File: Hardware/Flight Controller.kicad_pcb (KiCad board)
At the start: 6 copper layers, 47.5 x 47.5 mm, 159 parts, among them J1 USB4110GFA, J2 FPV, J3 ST_LINK, J4 GPS, J5 Airspeed sensor, J6 4in1 ESC, J7 RC Receiver, J8 VTX, J9 DJI, Q1 AO3407A, SW1 reset, SW2 MCU_BOOT, U1 TPS54302, U10 BMI270, U12 BMP388, U13 AT7456E, U14 SN65HVD230, U2 USBLC6-2SC6, U3 INA226, U4 AP63205WU, U5 AP2112K-3.3, U6 AP7343-33W5-7, U7 STM32H743VITx, U8 ICM-42688-P, U9 W25Q128JVSIQ, Y1 8MHz 12pF, Y2 27Mhz 20pF

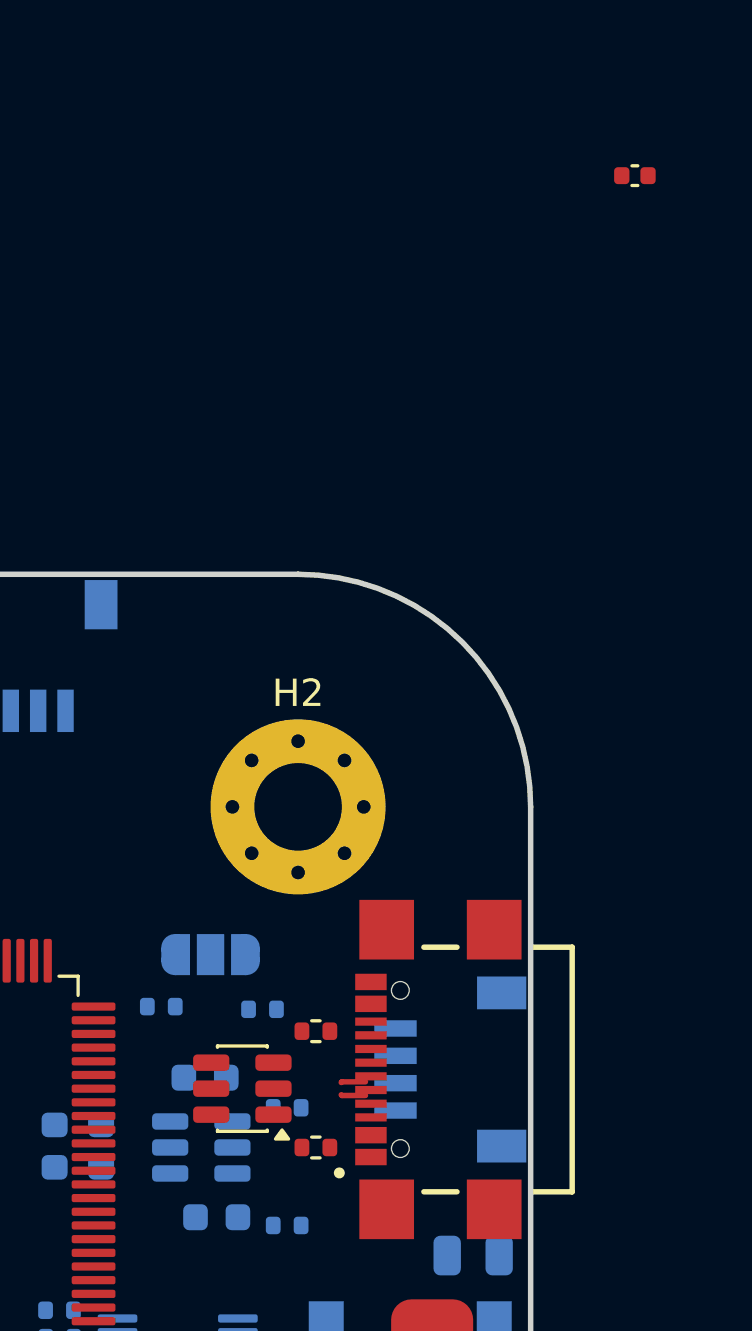
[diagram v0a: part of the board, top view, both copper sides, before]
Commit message: updated wiring of ESD from USB C
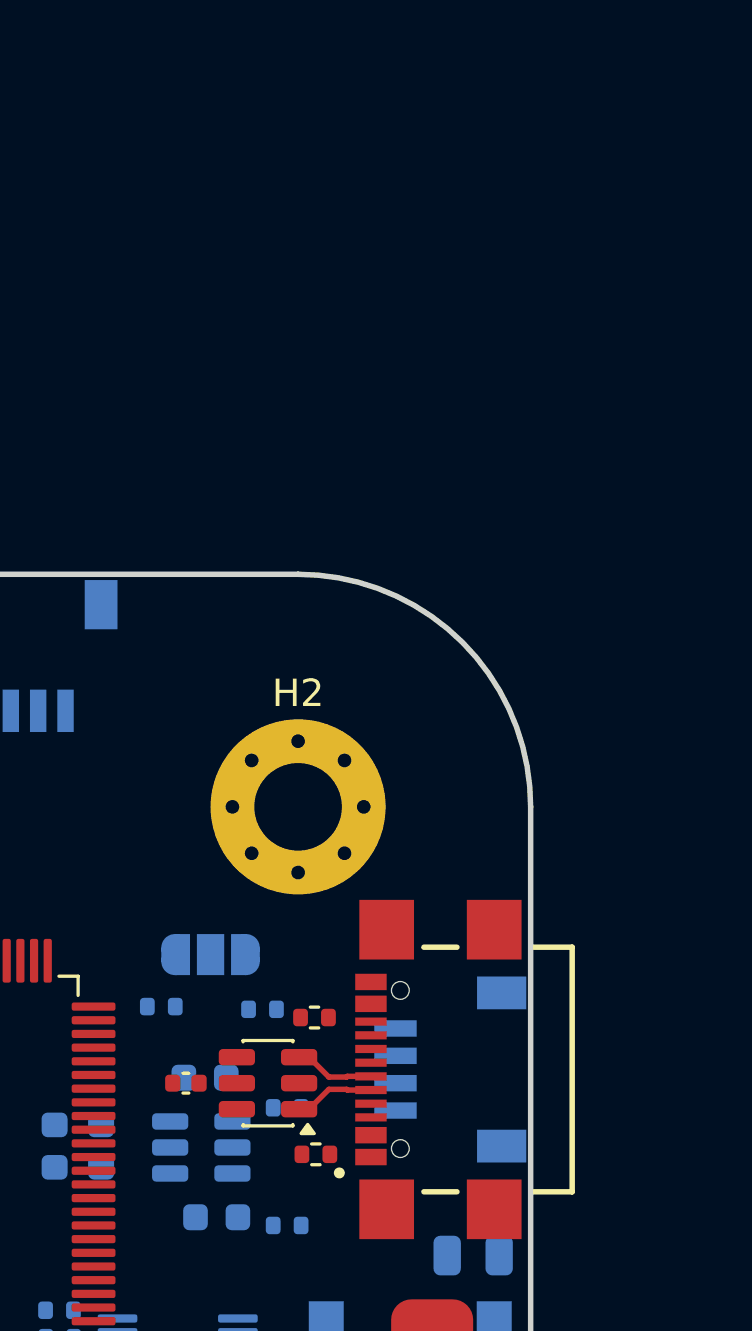
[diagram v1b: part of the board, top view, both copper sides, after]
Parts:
- moved C9 37.0 mm to (157.2, 92.3), turned to 180 degrees
- moved U2 0.96 mm to (160.2, 92.3)
- moved R2 0.50 mm to (161.9, 89.9)
- moved R1 0.25 mm to (161.9, 94.9)
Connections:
- U2 pad 1: /Power/D+ -> /Power/D-
- U2 pad 3: /Power/D- -> /Power/D+
- U2 pad 4: USB_DN -> USB_DP
- U2 pad 6: USB_DP -> USB_DN
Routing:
- net /Power/D+: track 0.90 -> 2.94 mm
- net /Power/D-: track 0.90 -> 2.94 mm
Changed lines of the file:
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@@
 	(footprint "Capacitor_SMD:C_0402_1005Metric"
 		(layer "F.Cu")
-		(at 173.61 59.13)
+		(at 157.2 92.3 180)
 		(descr "Capacitor SMD 0402 (1005 Metric), square (rectangular) end terminal, IPC-7351 nominal, (Body size source: IPC-SM-782 page 76, https://www.pcb-3d.com/wordpress/wp-content/uploads/ipc-sm-782a_amendment_1_and_2.pdf), generated with kicad-footprint-generator")
 		(tags "capacitor")
@@
 		(attr smd)
 		(fp_line
-			(start -0.107836 -0.36)
-			(end 0.107836 -0.36)
+			(start -0.107836 0.36)
+			(end 0.107836 0.36)
 			(stroke
 				(width 0.12)
@@
 		)
 		(fp_line
-			(start -0.107836 0.36)
-			(end 0.107836 0.36)
+			(start -0.107836 -0.36)
+			(end 0.107836 -0.36)
 			(stroke
 				(width 0.12)
@@
 		)
 		(fp_line
-			(start -0.91 -0.46)
-			(end 0.91 -0.46)
+			(start 0.91 0.46)
+			(end -0.91 0.46)
 			(stroke
 				(width 0.05)
@@
 		)
 		(fp_line
-			(start -0.91 0.46)
-			(end -0.91 -0.46)
+			(start 0.91 -0.46)
+			(end 0.91 0.46)
 			(stroke
 				(width 0.05)
@@
 		)
 		(fp_line
-			(start 0.91 -0.46)
-			(end 0.91 0.46)
+			(start -0.91 0.46)
+			(end -0.91 -0.46)
 			(stroke
 				(width 0.05)
@@
 		)
 		(fp_line
-			(start 0.91 0.46)
-			(end -0.91 0.46)
+			(start -0.91 -0.46)
+			(end 0.91 -0.46)
 			(stroke
 				(width 0.05)
@@
 		)
 		(fp_line
-			(start -0.5 -0.25)
-			(end 0.5 -0.25)
+			(start 0.5 0.25)
+			(end -0.5 0.25)
 			(stroke
 				(width 0.1)
@@
 		)
 		(fp_line
-			(start -0.5 0.25)
-			(end -0.5 -0.25)
+			(start 0.5 -0.25)
+			(end 0.5 0.25)
 			(stroke
 				(width 0.1)
@@
 		)
 		(fp_line
-			(start 0.5 -0.25)
-			(end 0.5 0.25)
+			(start -0.5 0.25)
+			(end -0.5 -0.25)
 			(stroke
 				(width 0.1)
@@
 		)
 		(fp_line
-			(start 0.5 0.25)
-			(end -0.5 0.25)
+			(start -0.5 -0.25)
+			(end 0.5 -0.25)
 			(stroke
 				(width 0.1)
@@
 		)
 		(pad "1" smd roundrect
-			(at -0.48 0)
+			(at -0.48 0 180)
 			(size 0.56 0.62)
 			(layers "F.Cu" "F.Mask" "F.Paste")
@@
 		)
 		(pad "2" smd roundrect
-			(at 0.48 0)
+			(at 0.48 0 180)
 			(size 0.56 0.62)
 			(layers "F.Cu" "F.Mask" "F.Paste")
@@
 	(footprint "Resistor_SMD:R_0402_1005Metric"
 		(layer "F.Cu")
-		(at 161.95 94.65)
+		(at 161.95 94.9)
 		(descr "Resistor SMD 0402 (1005 Metric), square (rectangular) end terminal, IPC-7351 nominal, (Body size source: IPC-SM-782 page 72, https://www.pcb-3d.com/wordpress/wp-content/uploads/ipc-sm-782a_amendment_1_and_2.pdf), generated with kicad-footprint-generator")
 		(tags "resistor")
@@
 	(footprint "Resistor_SMD:R_0402_1005Metric"
 		(layer "F.Cu")
-		(at 161.95 90.4)
+		(at 161.9 89.9)
 		(descr "Resistor SMD 0402 (1005 Metric), square (rectangular) end terminal, IPC-7351 nominal, (Body size source: IPC-SM-782 page 72, https://www.pcb-3d.com/wordpress/wp-content/uploads/ipc-sm-782a_amendment_1_and_2.pdf), generated with kicad-footprint-generator")
 		(tags "resistor")
@@
 	(footprint "Package_TO_SOT_SMD:SOT-23-6"
 		(layer "F.Cu")
-		(at 159.2625 92.5 180)
+		(at 160.2 92.3 180)
 		(descr "SOT, 6 Pin (JEDEC MO-178 Var AB https://www.jedec.org/document_search?search_api_views_fulltext=MO-178), generated with kicad-footprint-generator ipc_gullwing_generator.py")
 		(tags "SOT TO_SOT_SMD")
@@
 			(layers "F.Cu" "F.Mask" "F.Paste")
 			(roundrect_rratio 0.25)
-			(net 117 "/Power/D+")
+			(net 116 "/Power/D-")
 			(pinfunction "I/O1")
 			(pintype "passive")
@@
 			(layers "F.Cu" "F.Mask" "F.Paste")
 			(roundrect_rratio 0.25)
-			(net 116 "/Power/D-")
+			(net 117 "/Power/D+")
 			(pinfunction "I/O2")
 			(pintype "passive")
@@
 			(layers "F.Cu" "F.Mask" "F.Paste")
 			(roundrect_rratio 0.25)
-			(net 39 "USB_DN")
+			(net 38 "USB_DP")
 			(pinfunction "I/O2")
 			(pintype "passive")
@@
 			(layers "F.Cu" "F.Mask" "F.Paste")
 			(roundrect_rratio 0.25)
-			(net 38 "USB_DP")
+			(net 39 "USB_DN")
 			(pinfunction "I/O1")
 			(pintype "passive")
@@
 	)
 	(segment
-		(start 162.899999 92.75)
-		(end 163.7625 92.75)
+		(start 161.3375 93.25)
+		(end 161.7 93.25)
+		(width 0.2)
+		(layer "F.Cu")
+		(net 116)
+	)
+	(segment
+		(start 163.099999 92.55)
+		(end 163.9625 92.55)
+		(width 0.2)
+		(layer "F.Cu")
+		(net 116)
+	)
+	(segment
+		(start 161.7 93.25)
+		(end 162.425 92.525)
 		(width 0.2)
 		(layer "F.Cu")
@@
 	)
 	(segment
-		(start 162.874999 92.725)
-		(end 162.899999 92.75)
+		(start 163.074999 92.525)
+		(end 163.099999 92.55)
 		(width 0.2)
 		(layer "F.Cu")
@@
 	)
 	(segment
-		(start 162.899999 92.25)
-		(end 163.7625 92.25)
+		(start 162.425 92.525)
+		(end 163.074999 92.525)
+		(width 0.2)
+		(layer "F.Cu")
+		(net 116)
+	)
+	(segment
+		(start 161.7 91.35)
+		(end 162.425 92.075)
+		(width 0.2)
+		(layer "F.Cu")
+		(net 117)
+	)
+	(segment
+		(start 162.425 92.075)
+		(end 163.074999 92.075)
+		(width 0.2)
+		(layer "F.Cu")
+		(net 117)
+	)
+	(segment
+		(start 163.099999 92.05)
+		(end 163.9625 92.05)
+		(width 0.2)
+		(layer "F.Cu")
+		(net 117)
+	)
+	(segment
+		(start 161.3375 91.35)
+		(end 161.7 91.35)
 		(width 0.2)
 		(layer "F.Cu")
@@
 	)
 	(segment
-		(start 162.874999 92.275)
-		(end 162.899999 92.25)
+		(start 163.074999 92.075)
+		(end 163.099999 92.05)
 		(width 0.2)
 		(layer "F.Cu")

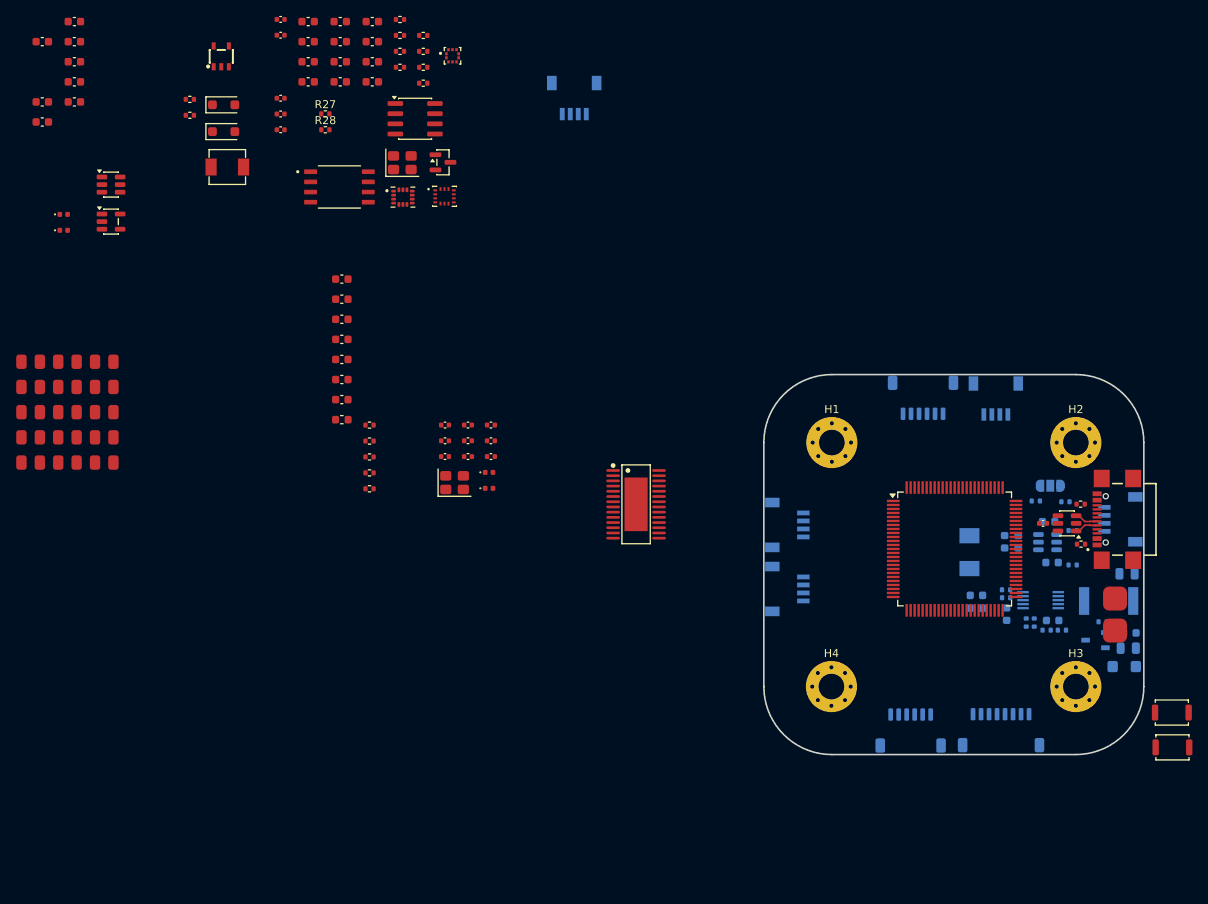
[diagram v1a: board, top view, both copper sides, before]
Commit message: Changed to CMOS, layout progress
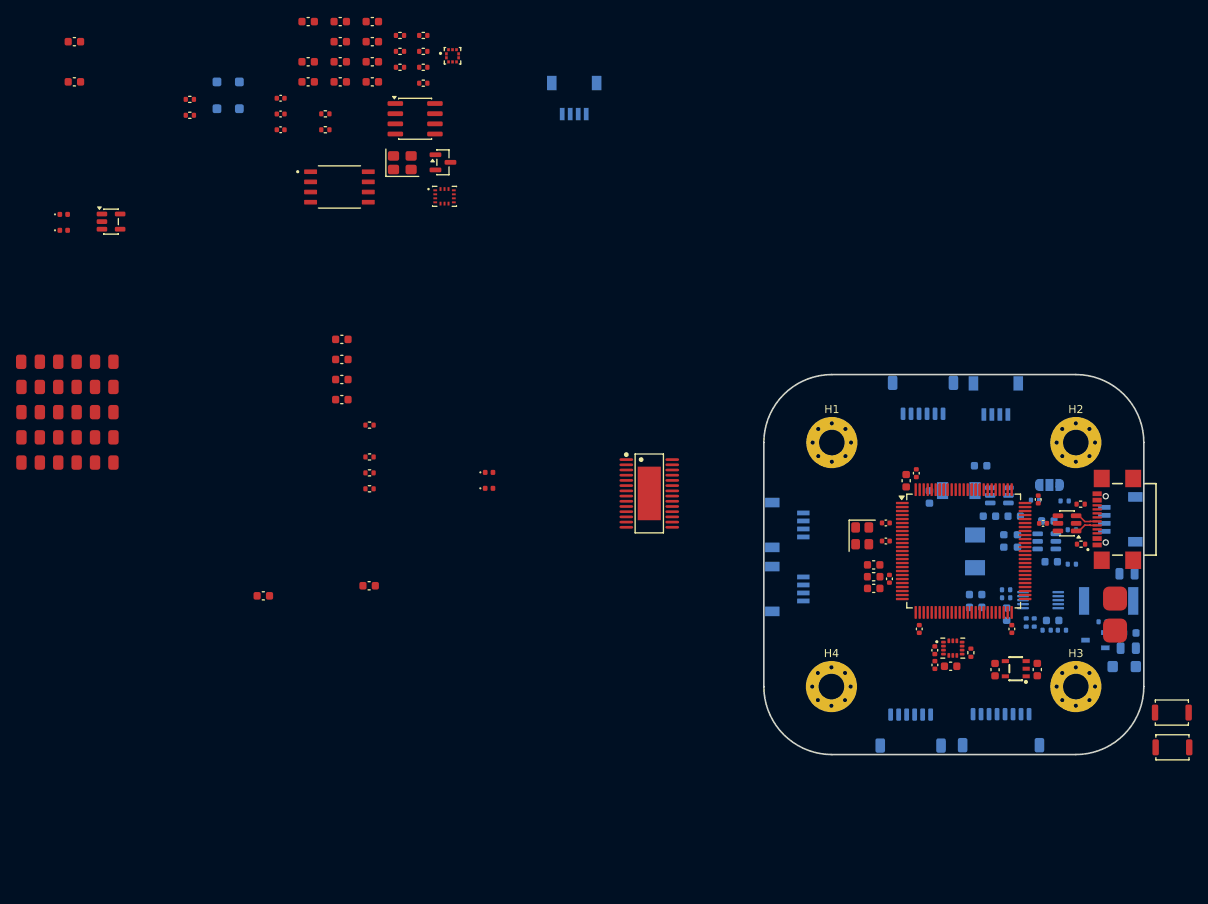
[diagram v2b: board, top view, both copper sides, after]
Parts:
- removed the C23 at (82.5, 80.0)
- removed the C32 at (88.2, 82.0)
- removed the R23 at (76.8, 29.3)
- added C21: 0.01uF, Capacitor_SMD:C_0603_1608Metric, F.Cu at (59.7, 101.4)
- added C21: 0.01uF, Capacitor_SMD:C_0603_1608Metric, F.Cu at (73.0, 100.1)
- C10, C14, C15, C16, D2, D3, L2, U4: moved to B.Cu
- C24, C31: value 27pF -> 0.1uF
- Y1: value 8MHz 12pF -> ASE-8.000MHZ-LC-T; footprint Crystal:Crystal_SMD_3225-4Pin_3.2x2.5mm -> Oscillator:Oscillator_SMD_Abracon_ASE-4Pin_3.2x2.5mm
- moved C18 142.3 mm to (156.5, 110.6), turned to 90 degrees
- moved C20 135.2 mm to (151.2, 110.6), turned to 90 degrees
- moved C10 135.2 mm to (153.6, 91.4)
- moved C15 128.2 mm to (150.5, 91.4), turned to 180 degrees
- moved C14 125.8 mm to (149.4, 85.1)
- moved U6 125.4 mm to (153.8, 110.5), turned to 90 degrees
- moved C16 122.3 mm to (143.0, 89.0), turned to 90 degrees
- moved U4 117.6 mm to (151.7, 88.8), turned to 180 degrees
- moved C36 113.6 mm to (143.7, 108.2), turned to 90 degrees
- moved C39 113.5 mm to (143.7, 110.0), turned to 90 degrees
- moved C38 112.0 mm to (145.7, 110.2)
- moved L2 100.0 mm to (146.7, 88.2)
- moved U8 88.9 mm to (145.9, 107.9)
- moved R19 79.7 mm to (148.2, 108.5), turned to 90 degrees
- moved C22 74.9 mm to (140.1, 87.0), turned to 90 degrees
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- renumbered C21 to C22, C22 to C23, C33 to C32, C34 to C33, C35 to C34, C36 to C35, C37 to C36, C38 to C37, C39 to C38, C40 to C39, C44 to C43, C45 to C44, C46 to C45, C47 to C46, C48 to C47, C49 to C48, C50 to C49, C51 to C50, C52 to C51, C53 to C52, C54 to C53, C55 to C54, C56 to C55, R13 to R10, R14 to R11, R15 to R12, R16 to R13, R17 to R14, R18 to R15, R20 to R16, R21 to R17, R22 to R18, R24 to R20, R25 to R21, R26 to R22, R27 to R23, R28 to R24, R29 to R25, R30 to R26, R31 to R27, R32 to R28, R5 to R3, R6 to R4, R7 to R5, R9 to R6, R10 to R7, R11 to R8, R12 to R9
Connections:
- C24 pad 1: HSE_IN -> +3.3V
- C31 pad 1: Net-(C31-Pad1) -> +3.3V
- R19 pad 1: Net-(C31-Pad1) -> GND
- R19 pad 2: HSE_OUT -> Net-(U8-INT2/FSYNC/CLKIN)
- U7 pad 13: HSE_OUT -> unconnected-(U7-PH1-Pad13)
- Y1 pad 1: HSE_IN -> +3.3V
- Y1 pad 3: Net-(C31-Pad1) -> HSE_IN
- Y1 pad 4: GND -> +3.3V

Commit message: added CAN connector
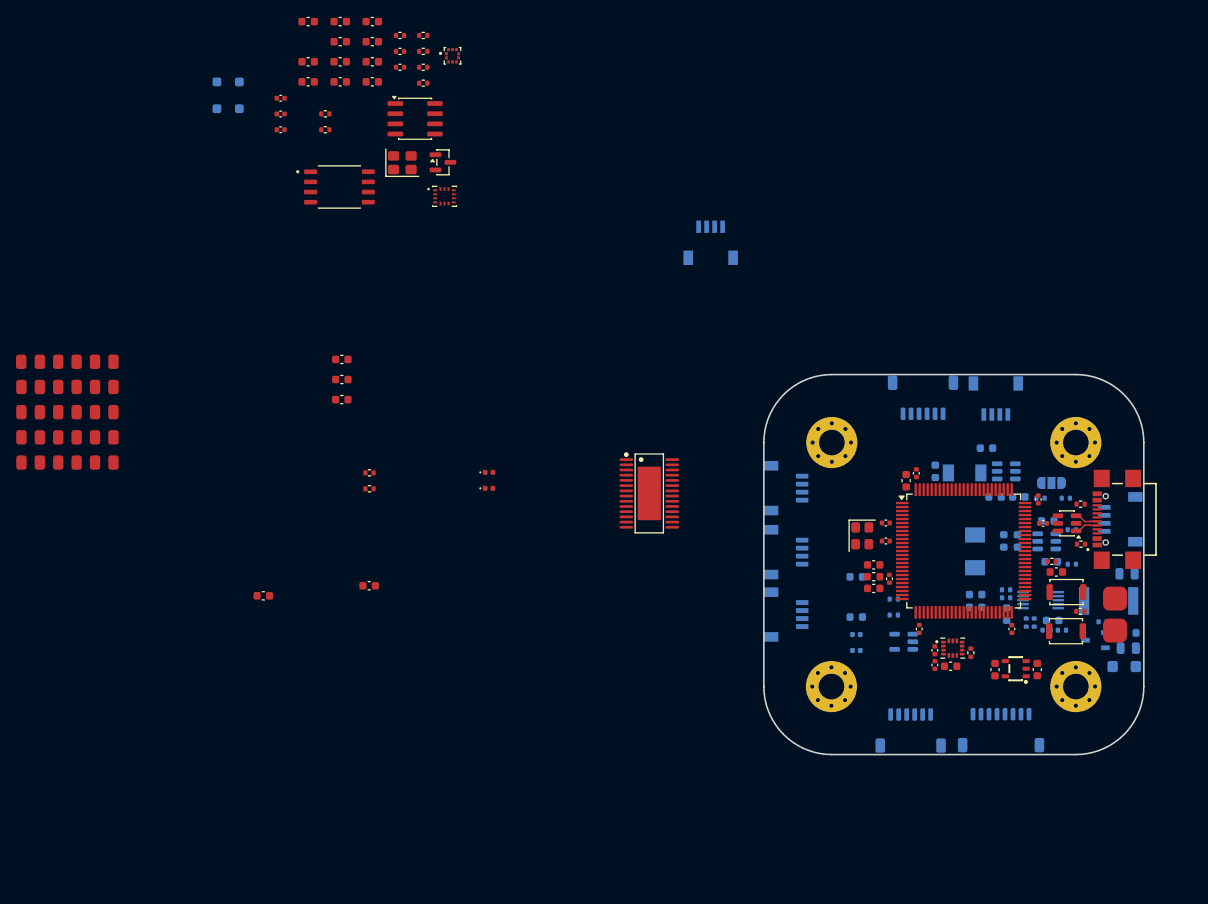
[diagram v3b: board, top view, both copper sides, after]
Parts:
- added J10: CAN BUS, memo:CONN-SMD_4P-P1.00_SM04B-SRSS-TB-LF-SN, B.Cu at (115.7, 57.2)
- C17, C19, D4, D5, R13, R14, U5: moved to B.Cu
- moved C17 118.4 mm to (133.8, 99.0), turned to 180 degrees
- moved C19 118.4 mm to (133.8, 104.0), turned to 180 degrees
- moved D4 112.1 mm to (133.9, 106.2), turned to 180 degrees
- moved D5 112.1 mm to (133.9, 108.2), turned to 180 degrees
- moved U5 112.1 mm to (139.8, 107.1), turned to 180 degrees
- moved R13 107.9 mm to (138.5, 101.8), turned to 180 degrees
- moved R14 107.9 mm to (138.5, 103.8), turned to 180 degrees
- moved C29 93.9 mm to (158.9, 98.4), turned to 180 degrees
- moved R15 91.8 mm to (161.9, 103.3)
- moved R16 86.3 mm to (158.3, 97.0)
- moved J2 69.8 mm to (125.2, 103.7), turned to 90 degrees
- moved SW1 23.5 mm to (160.1, 100.9)
- moved SW2 16.7 mm to (160.1, 105.8)
- moved J5 4.60 mm to (125.2, 87.9)
- moved J8 4.60 mm to (125.2, 95.9)
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
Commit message: added firmware drivers for all sensors for the test board
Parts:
- D4, R13: moved to F.Cu
- U13, U14: moved to B.Cu
- moved U14 74.1 mm to (139.3, 84.2), turned to 90 degrees
- moved U9 70.3 mm to (126.5, 91.1), turned to 90 degrees
- moved R13 60.7 mm to (86.2, 132.5), turned to 0 degrees
- moved D4 52.5 mm to (88.4, 132.5), turned to 0 degrees
- moved R17 49.3 mm to (86.2, 133.5)
- moved R18 48.4 mm to (86.2, 134.5)
- moved D6 47.6 mm to (88.4, 133.5)
- moved D7 46.6 mm to (88.4, 134.5)
- moved U13 31.8 mm to (139.2, 94.2), turned to 90 degrees
- moved J10 30.8 mm to (139.2, 76.9), turned to 0 degrees
- moved C17 8.87 mm to (141.3, 103.8), turned to 0 degrees
- moved J4 5.30 mm to (147.5, 76.8)
- moved J3 4.45 mm to (155.8, 76.8)
- moved J5 1.31 mm to (125.3, 89.2)
- moved J8 0.62 mm to (125.3, 96.5)
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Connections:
- J10 pad 2: CANH -> CANL
- J10 pad 3: CANL -> CANH

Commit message: progress layout
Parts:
- added Y3: ASE-27.000MHZ-LC-T, Oscillator:Oscillator_SMD_Abracon_ASE-4Pin_3.2x2.5mm, F.Cu at (59.1, 71.9)
- C2, C5: footprint Capacitor_SMD:C_0603_1608Metric -> Capacitor_SMD:C_0402_1005Metric
- C45, C47: footprint Capacitor_SMD:C_0603_1608Metric -> Capacitor_SMD:C_0402_1005Metric; moved to B.Cu
- C48, C49, C51, C52, C53, C54, R25, R26, Y2: moved to B.Cu
- D4: footprint LED_SMD:LED_0402_1005Metric -> LED_SMD:LED_0805_2012Metric
- D5, R14: moved to F.Cu
- moved C45 111.7 mm to (150.0, 106.8)
- moved C47 110.8 mm to (150.0, 108.1)
- moved C51 103.1 mm to (139.9, 108.3), turned to 180 degrees
- moved Y2 96.7 mm to (152.8, 107.5), turned to -90 degrees
- moved R25 96.3 mm to (137.9, 108.1), turned to 90 degrees
- moved C34 89.4 mm to (153.3, 105.7), turned to 180 degrees
- moved C35 87.3 mm to (156.1, 88.5), turned to 180 degrees
- moved C48 62.1 mm to (101.7, 87.7), turned to 180 degrees
- moved C49 62.1 mm to (101.7, 90.2), turned to 180 degrees
- moved C52 62.1 mm to (105.7, 85.1), turned to 180 degrees
- moved C53 62.1 mm to (105.7, 87.7), turned to 180 degrees
- moved C54 62.1 mm to (105.7, 90.2), turned to 180 degrees
- moved R26 62.1 mm to (112.0, 86.3), turned to 180 degrees
- moved R14 59.2 mm to (86.2, 131.5), turned to 0 degrees
- moved D5 51.1 mm to (88.4, 131.5), turned to 0 degrees
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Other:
- rule pad_to_mask_clearance: 0.09 -> 0
